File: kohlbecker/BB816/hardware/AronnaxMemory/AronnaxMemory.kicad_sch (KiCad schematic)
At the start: 13 parts, among them J2 Conn_02x40_Odd_Even, J3 Conn_02x18_Odd_Even, U1 74LS04, U11 AS6C4008-55PCN, U12 AS6C4008-55PCN, U13 AT28C256-15PC, U2 74LS32, U3 74LS32, U4 74LS32, U5 74LS08, U6 74LS138, U7 74LS138, U8 74LS138

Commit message: Before deleting high memory
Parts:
- added C1, C10, C11, C2, C3, C4, C5, C6, C7, C8, C9: 100nF, symbol Device:C
- added C12: 220u, Capacitor_THT:CP_Radial_D6.3mm_P2.50mm, symbol Device:C_Polarized_Small
- added C13: 10u, Capacitor_THT:CP_Radial_D4.0mm_P1.50mm, symbol Device:C_Polarized_Small
- added D1: POWER, LED_THT:LED_D3.0mm, symbol Device:LED_Small
- added J1: Barrel_Jack_Switch, Connector_BarrelJack:BarrelJack_Horizontal, symbol Connector:Barrel_Jack_Switch
- added J4: Conn_02x16_Odd_Even, Connector_PinHeader_2.54mm:PinHeader_2x16_P2.54mm_Vertical, symbol Connector_Generic:Conn_02x16_Odd_Even
- added R6: 1k, Resistor_THT:R_Axial_DIN0207_L6.3mm_D2.5mm_P7.62mm_Horizontal, symbol Device:R_Small
- added unit 5 of U5
- U1, U2, U3, U4, U5: footprint (none) -> Package_DIP:DIP-14_W7.62mm
- U13: footprint (none) -> Socket:DIP_Socket-28_W11.9_W12.7_W15.24_W17.78_W18.5_3M_228-1277-00-0602J
- U6, U7, U8: footprint (none) -> Package_DIP:DIP-16_W7.62mm
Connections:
- net A14: no longer J3.3 (Pin_3), U11.27 (A8), U12.27 (A8), U13.25 (A8), U7.1 (A0)
- net GND: now also U1.7 (GND), U2.7 (GND), U3.7 (GND), U4.7 (GND), C1.2, C10.2, C11.2, C12.2, C13.2, C2.2, C3.2, C4.2, C5.2, C6.2, C7.2, C8.2, C9.2, D1.1 (K), J1.2, J4.10 (Pin_10), J4.12 (Pin_12), J4.14 (Pin_14), J4.16 (Pin_16), J4.18 (Pin_18), J4.2 (Pin_2), J4.20 (Pin_20), J4.22 (Pin_22), J4.24 (Pin_24), J4.26 (Pin_26), J4.28 (Pin_28), J4.30 (Pin_30), J4.32 (Pin_32), J4.4 (Pin_4), J4.6 (Pin_6), J4.8 (Pin_8), U5.7 (GND)
- net MEG0: now also J4.3 (Pin_3)
- net VCC: now also U1.14 (VCC), U11.32 (VCC), U12.32 (VCC), U13.28 (VCC), U2.14 (VCC), U3.14 (VCC), U4.14 (VCC), U8.16 (VCC), U8.6 (E3), C1.1, C10.1, C11.1, C12.1, C13.1, C2.1, C3.1, C4.1, C5.1, C6.1, C7.1, C8.1, C9.1, J1.1, R6.2, U5.14 (VCC)
- net ~{0x00}: now also J4.31 (Pin_31)
- net ~{0x20}: now also J4.29 (Pin_29)
- net ~{0x40}: now also J4.27 (Pin_27)
- net ~{0x60}: now also J4.25 (Pin_25)
- net ~{0x80}: now also J4.23 (Pin_23)
- net ~{0xA0}: now also J4.21 (Pin_21)
- net ~{0xCO}: now also J4.19 (Pin_19)
- net ~{0xE0}: now also J4.17 (Pin_17)
- net ~{BANK0_HI}: now also J4.9 (Pin_9)
- net ~{BANK0_LO}: now also J4.11 (Pin_11)
- net ~{MEG0}: now also J4.1 (Pin_1)
- net ~{PAGE1}: now also J4.15 (Pin_15)
- net ~{ROM_OE}: now also J4.13 (Pin_13)
- net ~{MEG0LO}: now reaches U12.22 (CE#), U3.3
- net ~{MEG0HI}: now reaches U11.22 (CE#), U2.11
- net at U8.4 (E1): now also U8.8 (GND)
- new net: D1.2 (A), R6.1
- new net A8: J3.3 (Pin_3), U11.27 (A8), U12.27 (A8), U13.25 (A8), U7.1 (A0)
- new net ~{MEG0_HI}: J4.5 (Pin_5)
- new net ~{MEG0_LO}: J4.7 (Pin_7)
- no-connect marks 14 -> 15
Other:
- note added: "BB816"
- note added: "POWER"
- note removed: "OUTPUT"
- moved on the sheet: J2, J3, U11, U12, U13, U1A, U1B, U1C, U1D, U1E, U1F, U1G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

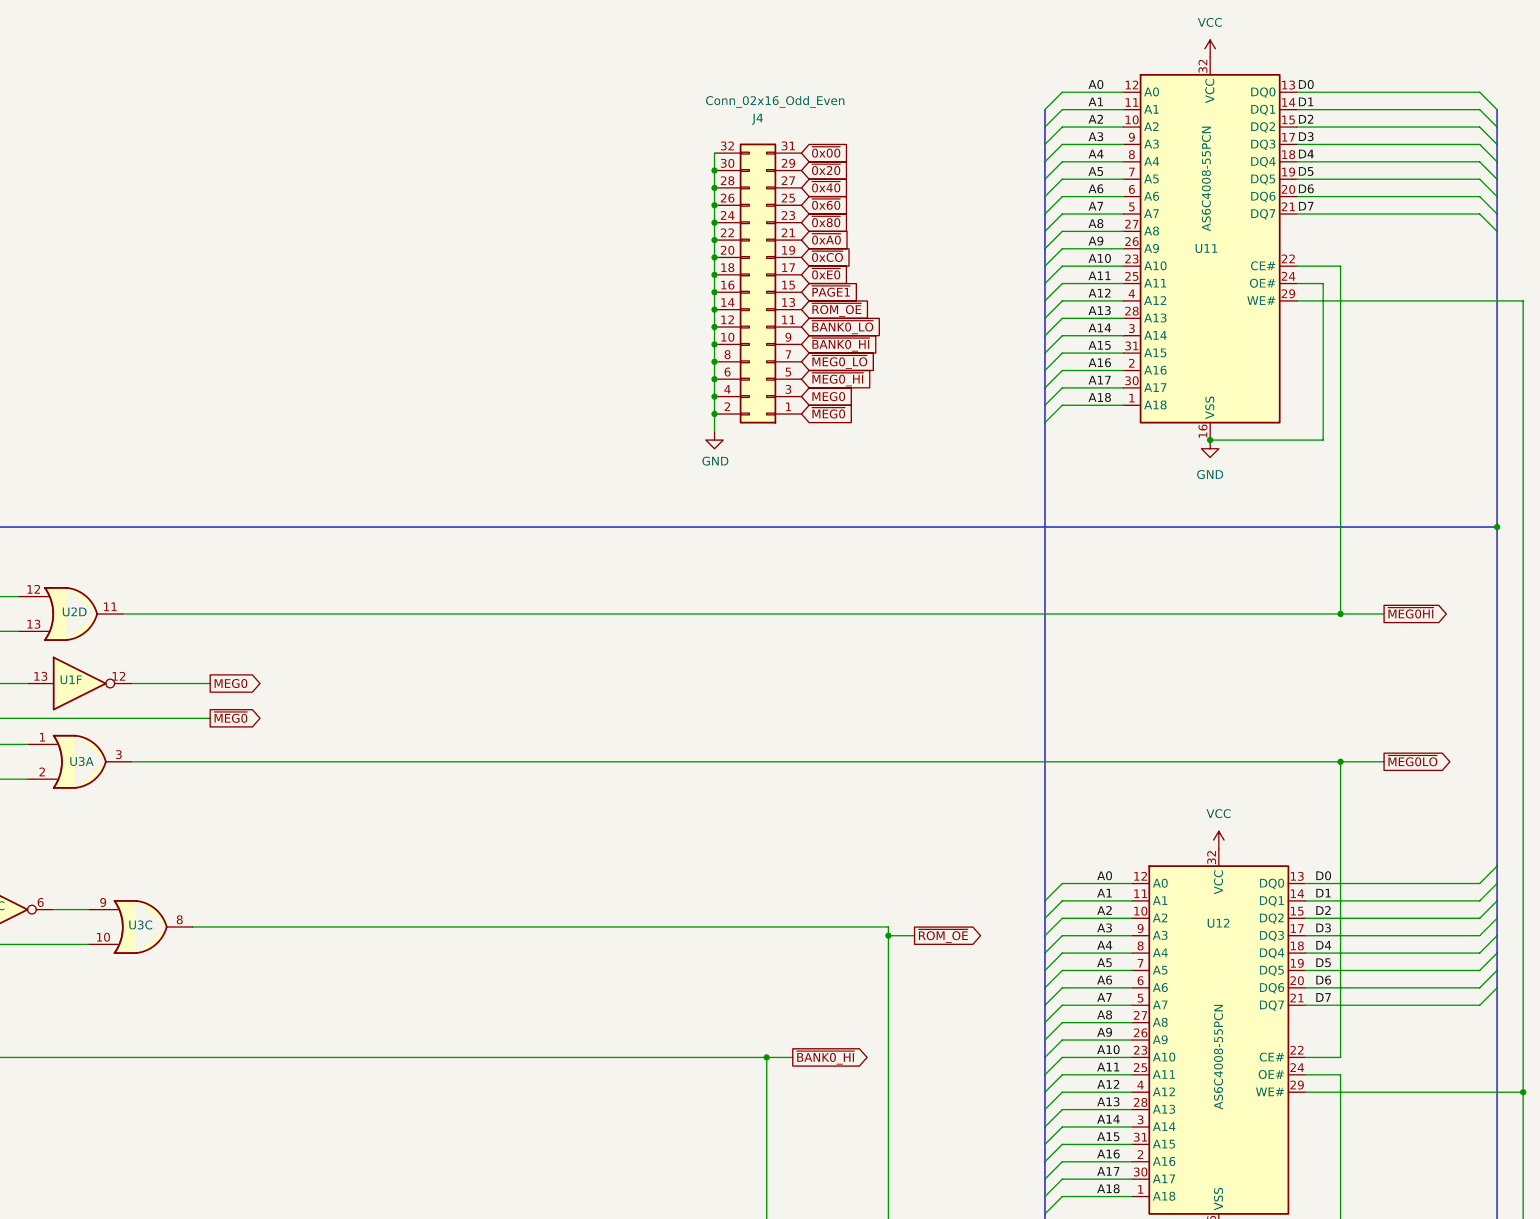
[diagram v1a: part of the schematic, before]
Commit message: Delete hi ram
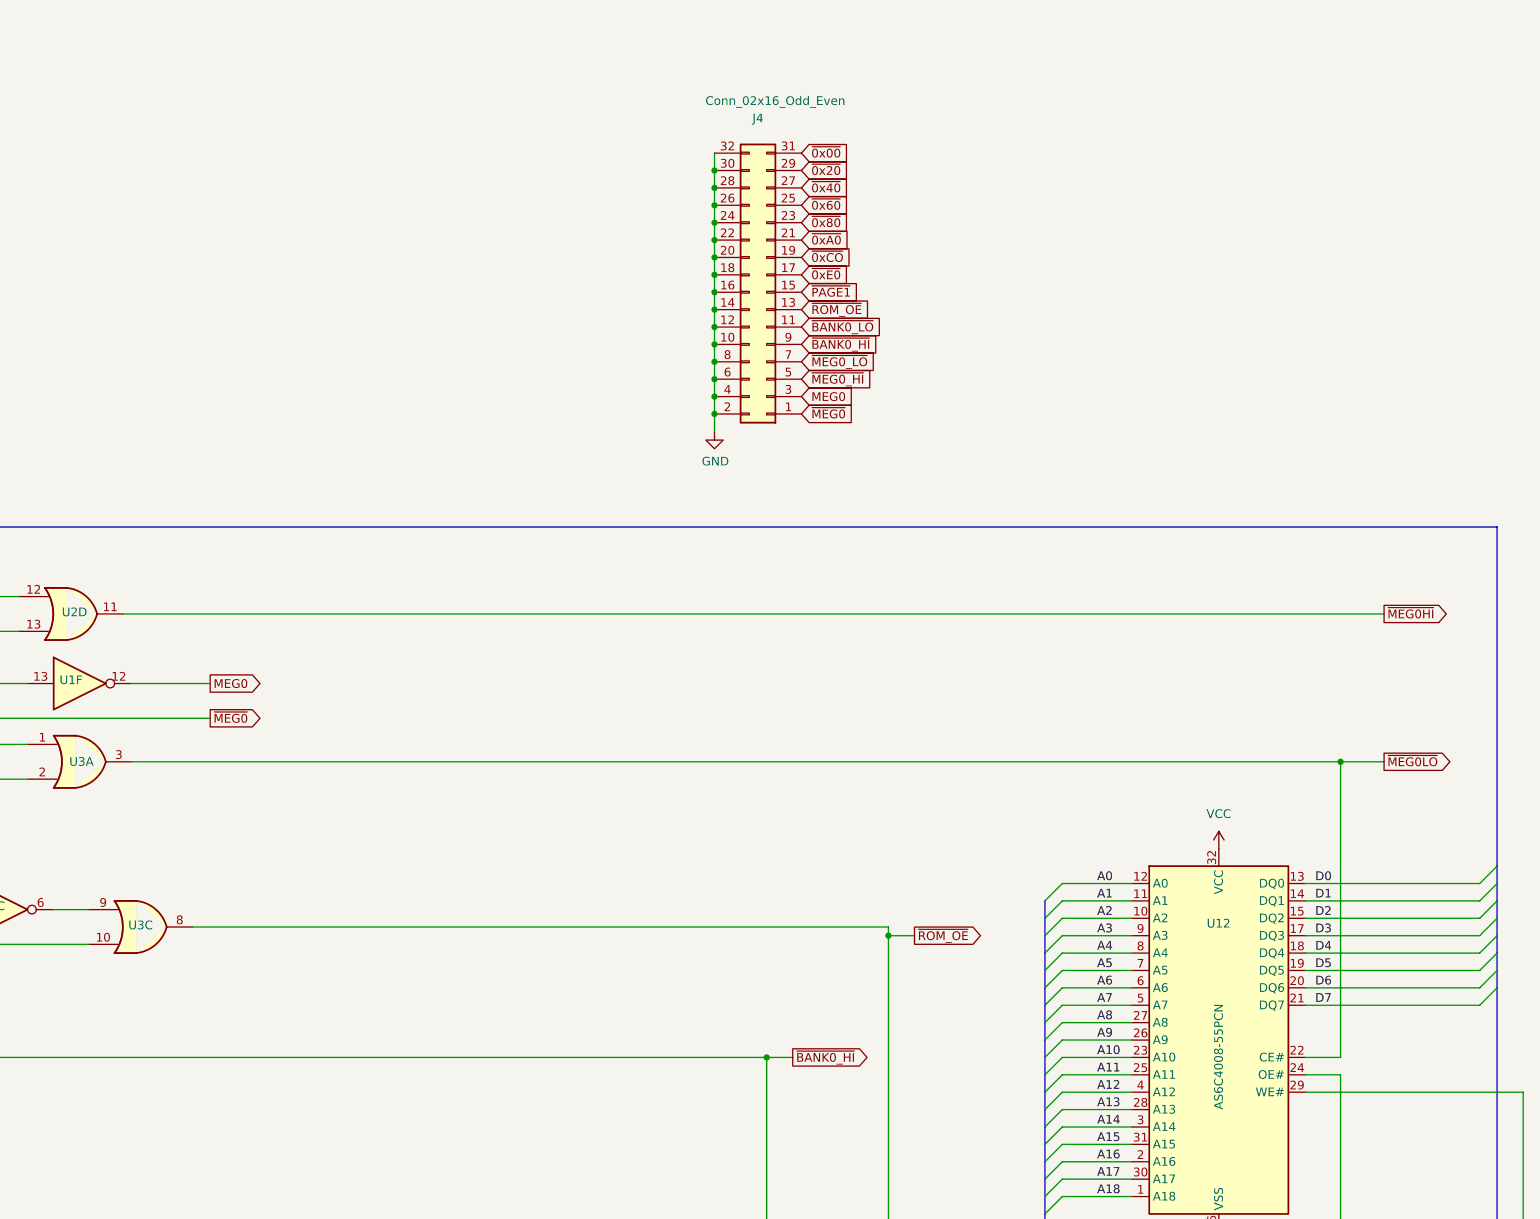
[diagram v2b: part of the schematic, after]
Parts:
- removed U11: AS6C4008-55PCN, Package_DIP:DIP-32_W15.24mm, symbol Memory_RAM:AS6C4008-55PCN

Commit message: Ready update schematic with added components to breakout
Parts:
- removed unit 4 of U2
- removed unit 5 of U4
- added R11: 3.3k, Resistor_THT:R_Axial_DIN0207_L6.3mm_D2.5mm_P7.62mm_Horizontal, symbol Device:R_Small
- added R12: 100k, Resistor_THT:R_Axial_DIN0207_L6.3mm_D2.5mm_P7.62mm_Horizontal, symbol Device:R_Small
- added U10: 74AHC125, Package_DIP:DIP-14_W7.62mm, symbol 74xx:74LS125
- added U11, U5: 74LS32, Package_DIP:DIP-14_W7.62mm, symbol 74xx:74LS32
- added U9: 74HC74, Package_DIP:DIP-14_W7.62mm, symbol 74xx:74LS74
- added X1: 8MHz, Oscillator:Oscillator_DIP-8, symbol Oscillator:CXO_DIP8
- added X3: 16MHz, Oscillator:Oscillator_DIP-8, symbol Oscillator:CXO_DIP8
- renumbered U3 to U2, U4 to U3, U5 to U4
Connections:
- net A15: now also U1.5, U3.10; no longer U1.3, U3.13
- net A19: now also U2.13; no longer U1.1, U2.2
- net CLK_SRC: now also R12.1, U10.8
- net E: now also U1.13, U1.3, X1.1 (EN); no longer U1.5
- net GND: now also R11.2, R12.2, U5.7 (GND), X1.4 (GND), X3.4 (GND)
- net VCC: now also U5.14 (VCC), U9.10 (~{S}), U9.13 (~{R}), X1.8 (Vcc), X3.8 (Vcc)
- net ~{BANK0_HI}: now also U3.2; no longer U3.10
- net ~{BANK0_LO}: now also U3.8; no longer U3.11
- net ~{BANK0}: now also U3.9; no longer U3.12
- net ~{CLK_EN}: now also R11.1, U10.10
- net ~{MEG0_LO}: now also J4.1 (Pin_1), U1.1, U12.22 (CE#), U2.11; no longer J4.7 (Pin_7)
- net ~{ROM_OE}: now also U3.3; no longer U3.8
- net MEG0_LO: now reaches U1.2
- net MEG0_LO: now also J4.3 (Pin_3)
- net at U3.4: now also U1.6; no longer U1.4
- net at U12.24 (OE#): now also U3.11; no longer U3.3
- net at U4.3: now also U3.12; no longer U3.1
- net at U1.10: now also U3.13; no longer U3.2
- net MEG0: no longer names the net of U1.12
- net MEG0: now also X3.1 (EN); no longer J4.3 (Pin_3)
- removed net ~{MEG0LO}: U12.22 (CE#), U2.3
- net ~{MEG0_HI}: no longer names the net of J4.5 (Pin_5)
- removed net ~{MEG0}: J4.1 (Pin_1), U1.13, U2.1, U2.8
- new net: U11.3, U9.11 (C)
- new net: U9.12 (D), U9.8 (~{Q})
- new net: U10.9, U9.9 (Q)
- new net: U2.12, U2.8
- new net: U1.4, U3.1
- new net 16MHz: U11.1, X3.5 (OUT)
- new net 8MHz: U11.2, X1.5 (OUT)
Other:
- note added: "CLOCK"
- moved on the sheet: J2, J3, J4, U12, U13, U1A, U1B, U1C, U1D, U1E, U1F, U2A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

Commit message: Memory
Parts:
- removed J4: Conn_02x16_Odd_Even, Connector_PinHeader_2.54mm:PinHeader_2x16_P2.54mm_Vertical, symbol Connector_Generic:Conn_02x16_Odd_Even
- removed R11: 3.3k, Resistor_THT:R_Axial_DIN0207_L6.3mm_D2.5mm_P7.62mm_Horizontal, symbol Device:R_Small
- removed R12: 100k, Resistor_THT:R_Axial_DIN0207_L6.3mm_D2.5mm_P7.62mm_Horizontal, symbol Device:R_Small
- removed unit 6 of U1
- removed U10: 74AHC125, Package_DIP:DIP-14_W7.62mm, symbol 74xx:74LS125
- removed U11: 74LS32, Package_DIP:DIP-14_W7.62mm, symbol 74xx:74LS32
- removed U9: 74HC74, Package_DIP:DIP-14_W7.62mm, symbol 74xx:74LS74
- removed X1: 8MHz, Oscillator:Oscillator_DIP-8, symbol Oscillator:CXO_DIP8
- removed X3: 16MHz, Oscillator:Oscillator_DIP-8, symbol Oscillator:CXO_DIP8
- added J5, J6: I/O ~{CS}, Connector_PinHeader_2.54mm:PinHeader_2x16_P2.54mm_Vertical, symbol Connector_Generic:Conn_02x08_Odd_Even
- added J9: Vector Rewrite, Connector_PinHeader_2.54mm:PinHeader_2x16_P2.54mm_Vertical, symbol Connector_Generic:Conn_02x12_Odd_Even
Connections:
- net A1: now also J9.15 (Pin_15); no longer J3.17 (Pin_17)
- net A2: now also J9.13 (Pin_13); no longer J3.15 (Pin_15)
- net A3: now also J9.11 (Pin_11); no longer J3.13 (Pin_13)
- net A4: now also J9.9 (Pin_9); no longer J3.11 (Pin_11)
- net E: now also J9.6 (Pin_6)
- net GND: now also J5.10 (Pin_10), J5.12 (Pin_12), J5.14 (Pin_14), J5.16 (Pin_16), J5.2 (Pin_2), J5.4 (Pin_4), J5.6 (Pin_6), J5.8 (Pin_8), J6.10 (Pin_10), J6.12 (Pin_12), J6.14 (Pin_14), J6.16 (Pin_16), J6.2 (Pin_2), J6.4 (Pin_4), J6.6 (Pin_6), J6.8 (Pin_8), J9.1 (Pin_1), J9.10 (Pin_10), J9.12 (Pin_12), J9.14 (Pin_14), J9.16 (Pin_16), J9.2 (Pin_2), J9.3 (Pin_3), J9.5 (Pin_5), J9.7 (Pin_7)
- net MEG0_LO: now also J6.3 (Pin_3)
- net VCC: now also J9.4 (Pin_4)
- net ~{0x00}: now also J5.15 (Pin_15)
- net ~{0x20}: now also J5.13 (Pin_13)
- net ~{0x40}: now also J5.11 (Pin_11)
- net ~{0x60}: now also J5.9 (Pin_9)
- net ~{0x80}: now also J5.7 (Pin_7)
- net ~{0xA0}: now also J5.5 (Pin_5)
- net ~{0xCO}: now also J5.3 (Pin_3)
- net ~{0xE0}: now also J5.1 (Pin_1)
- net ~{BANK0_HI}: now also J6.9 (Pin_9)
- net ~{BANK0_LO}: now also J6.11 (Pin_11)
- net ~{MEG0_LO}: now also J6.1 (Pin_1)
- net ~{PAGE1}: now also J6.15 (Pin_15)
- net ~{ROM_OE}: now also J6.13 (Pin_13)
- net ~{VP}: now also J9.8 (Pin_8)
- new net: J9.17 (Pin_17), J9.19 (Pin_19), J9.21 (Pin_21), J9.23 (Pin_23)
- new net AA1: J3.17 (Pin_17), J9.24 (Pin_24)
- new net AA2: J3.15 (Pin_15), J9.22 (Pin_22)
- new net AA3: J3.13 (Pin_13), J9.20 (Pin_20)
- new net AA4: J3.11 (Pin_11), J9.18 (Pin_18)
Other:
- note removed: "CLOCK"
- moved on the sheet: J2, J3, U2A, U2B, U2C, U2D
